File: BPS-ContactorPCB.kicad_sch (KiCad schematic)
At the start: 12 parts, among them J1 BPS_PWR, J2 BPS_IN, J3 DRV_ESTOP, J4 EXT_ESTOP, J5 HV+ Contactor, J6 HV- Contactor, U1 SFH617A-1

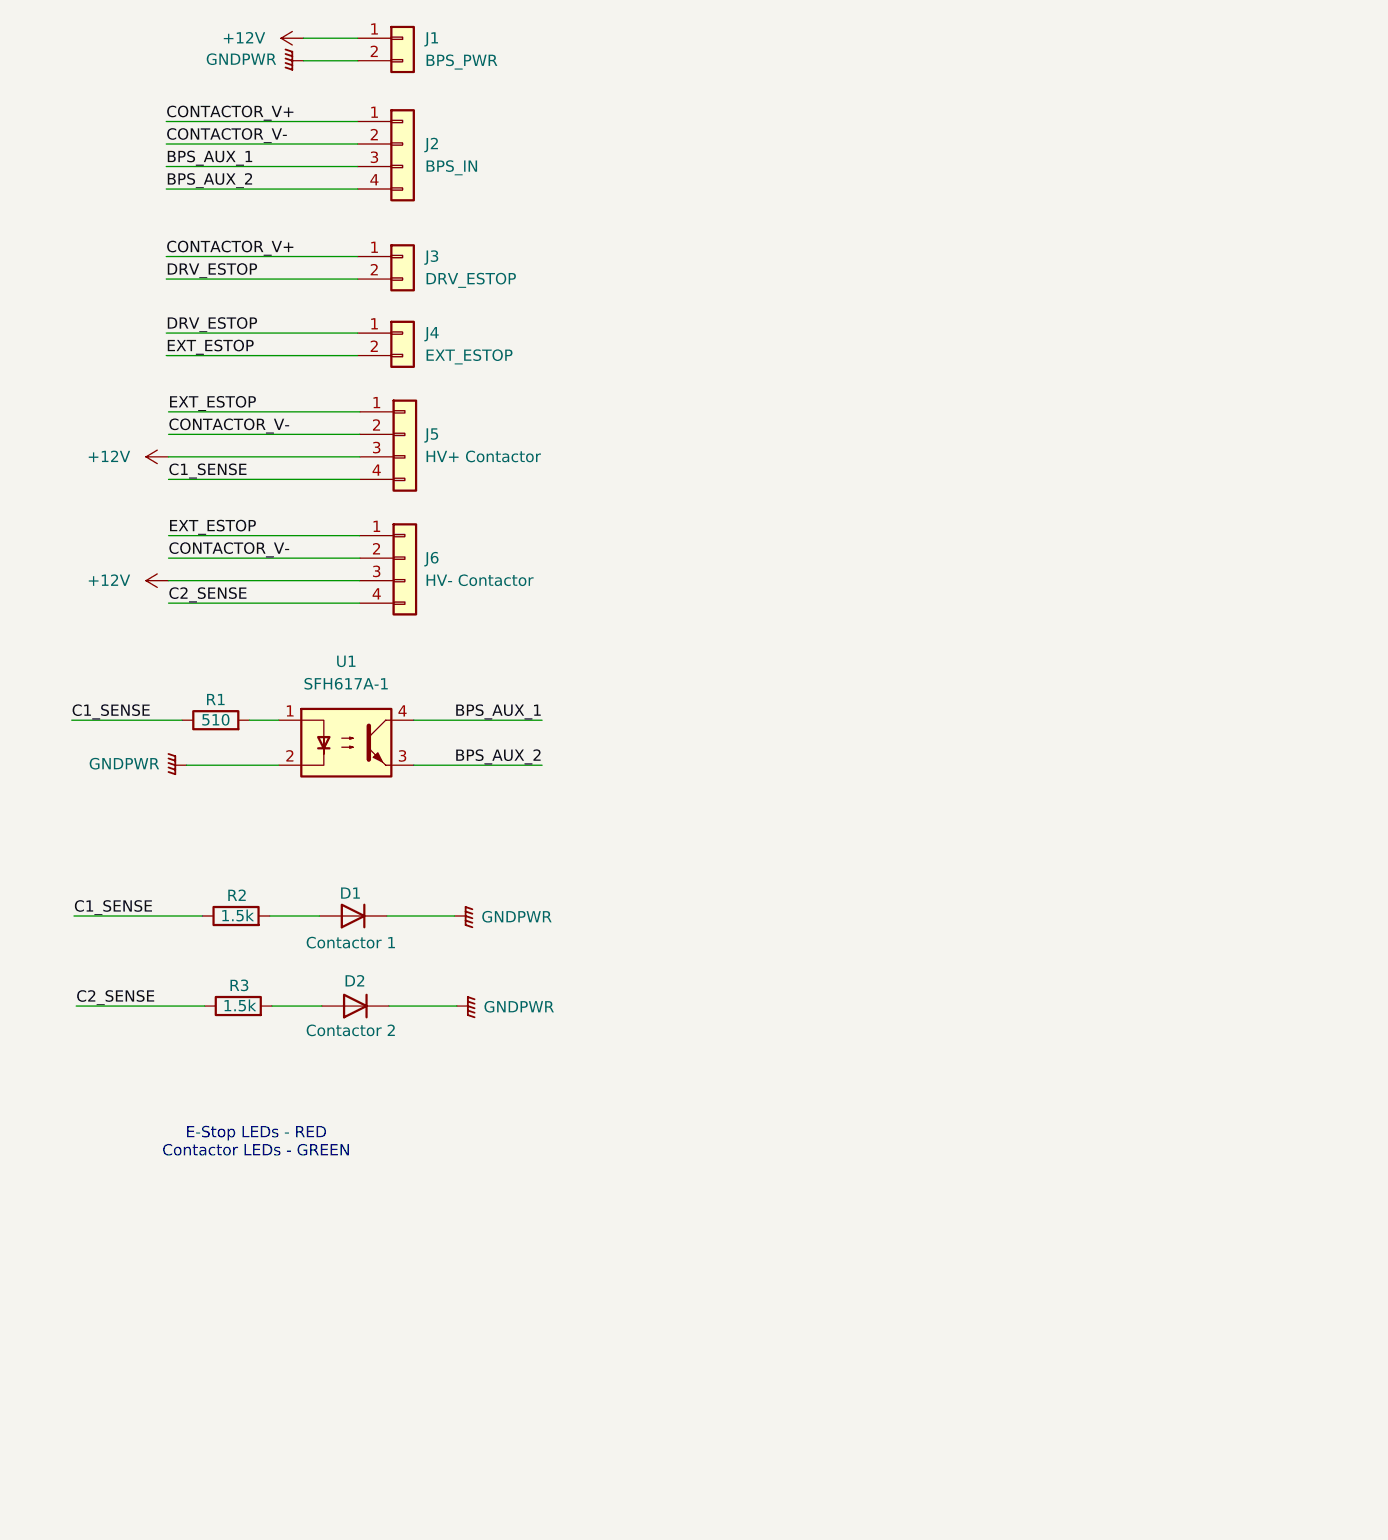
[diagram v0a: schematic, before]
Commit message: updated layout
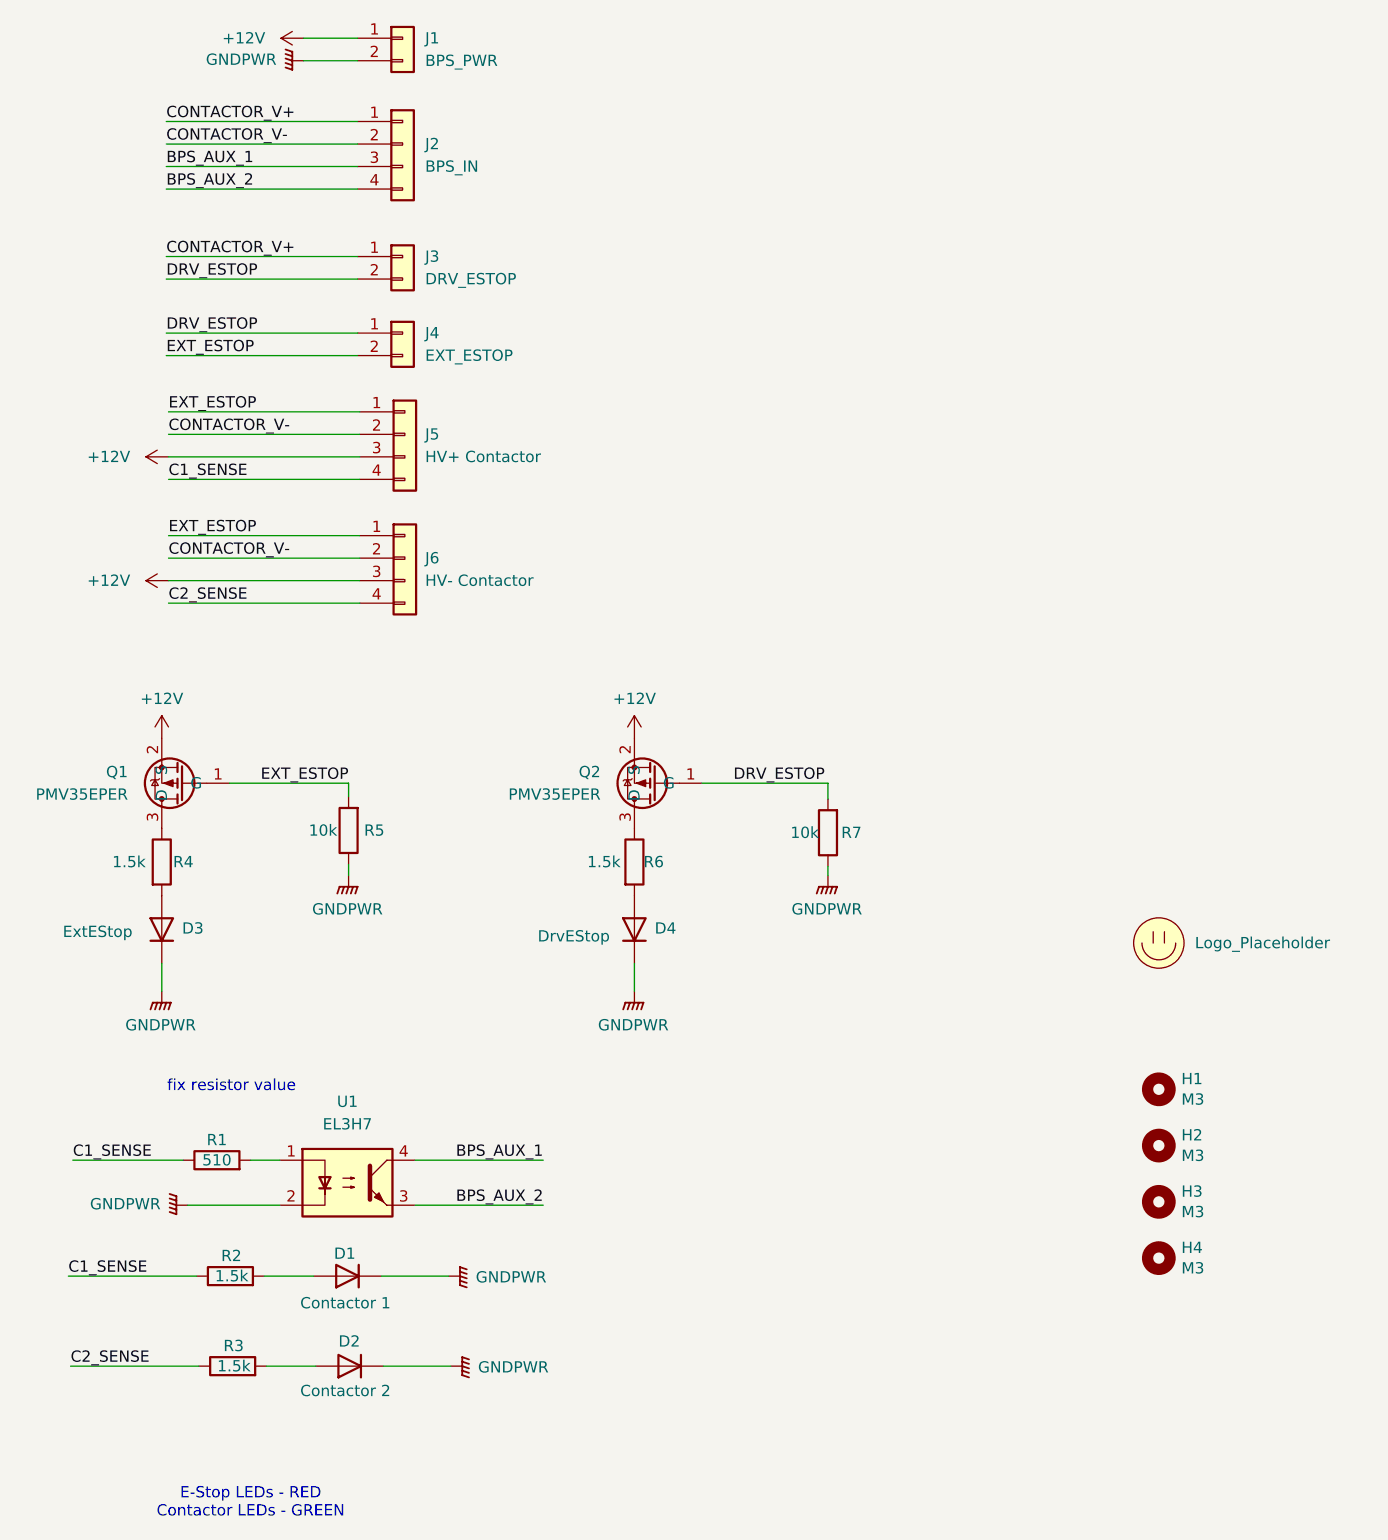
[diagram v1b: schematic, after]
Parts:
- added D3: ExtEStop, LED_SMD:LED_0805_2012Metric, symbol Device:D
- added D4: DrvEStop, LED_SMD:LED_0805_2012Metric, symbol Device:D
- added H1, H2, H3, H4: M3, MountingHole:MountingHole_3mm, symbol Mechanical:MountingHole
- added LOGO2: Logo_Placeholder, UTSVT_Special:Hallock_Image_Tiny, symbol utsvt-misc:Logo_Placeholder
- added Q1, Q2: PMV35EPER, Package_TO_SOT_SMD:SOT-23, symbol utsvt-chips:PMV35EPE
- added R4, R6: 1.5k, Resistor_SMD:R_0805_2012Metric, symbol Device:R
- added R5, R7: 10k, Resistor_SMD:R_0805_2012Metric, symbol Device:R
- R1: footprint (none) -> Resistor_SMD:R_0805_2012Metric
- U1: value SFH617A-1 -> EL3H7; footprint Package_DIP:DIP-4_W7.62mm -> Package_SO:SOP-4_4.4x2.6mm_P1.27mm
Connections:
- net +12V: now also Q1.2 (S), Q2.2 (S)
- net DRV_ESTOP: now also Q2.1 (G), R7.2
- net EXT_ESTOP: now also Q1.1 (G), R5.2
- net GNDPWR: now also D3.1 (K), D4.1 (K), R5.1, R7.1
- new net: D3.2 (A), R4.2
- new net: Q1.3 (D), R4.1
- new net: D4.2 (A), R6.2
- new net: Q2.3 (D), R6.1
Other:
- note added: "fix resistor value"
- moved on the sheet: D1, D2, R1, R2, R3, U1

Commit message: oops. done i hope
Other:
- note removed: "fix resistor value"
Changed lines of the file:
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@@
-		)
-	)
-	(text "fix resistor value"
-		(exclude_from_sim no)
-		(at 43.434 137.16 0)
-		(effects
-			(font
-				(size 1.27 1.27)
-			)
 		)
 	)
@@
 			)
 		)
-		(property "Datasheet" "http://www.vishay.com/docs/83740/sfh617a.pdf"
+		(property "Datasheet" "https://www.mouser.com/datasheet/2/143/EVER_S_A0005045010_1-2548609.pdf"
 			(at 56.515 147.955 0)
 			(effects
@@
 			)
 		)
-		(property "Description" "Optocoupler, Phototransistor Output, 5300 VRMS, VCEO 70V, CTR% 40-80, -55 to +110 degree Celsius, UL, BSI, FIMKO, cUL, THT PDIP-4"
+		(property "Description" ""
 			(at 56.515 147.955 0)
 			(effects
